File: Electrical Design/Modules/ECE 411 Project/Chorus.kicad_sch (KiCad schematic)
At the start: 42 parts, among them Q2 2N3904, Q3 2N3904, Q4 2N3904, U3 MN3207

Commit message: kicad business
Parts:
- renumbered V3207D to V3207D1, V3207D to V3207D2
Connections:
- net +V: no longer Q2.3 (C)
- net GND: now also R22.1
- new net 9V: Q2.3 (C)
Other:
- company: (none) -> Portland State University
- title: (none) -> Chorus Effect
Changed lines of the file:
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@@
 	(generator_version "8.0")
 	(paper "A4")
+	(title_block
+		(title "Chorus Effect")
+		(date "2024-10-31")
+		(rev "1.1")
+		(company "Portland State University")
+		(comment 1 "Open Source Hardware")
+		(comment 2 "Design: Eric Sanman, Sierra Buckley, Chuong Vo, Chris Crider")
+	)
 	(junction
 		(at 92.71 41.91)
@@
 		)
 	)
-	(global_label "+V"
-		(shape input)
-		(at 50.8 19.05 90)
-		(fields_autoplaced yes)
-		(effects
-			(font
-				(size 1.27 1.27)
-			)
-			(justify left)
-		)
-		(property "Intersheetrefs" "${INTERSHEET_REFS}"
-			(at 50.8 13.4038 90)
-			(effects
-				(font
-					(size 1.27 1.27)
-				)
-				(justify left)
-				(hide yes)
-			)
-		)
-	)
 	(global_label "Clock{slash}lfo from .uC"
 		(shape input)
@@
 		)
 	)
+	(hierarchical_label "9V"
+		(shape input)
+		(at 50.8 19.05 90)
+		(fields_autoplaced yes)
+		(effects
+			(font
+				(size 1.27 1.27)
+			)
+			(justify left)
+		)
+	)
 	(symbol
 		(lib_id "Device:R")
@@
 		(dnp no)
 		(fields_autoplaced yes)
-		(property "Reference" "V3207D"
+		(property "Reference" "V3207D2"
 			(at 156.21 141.0014 0)
 			(effects
@@
 			(project "ECE 411 Project"
 				(path "/2625e5a1-d0c8-41ce-941d-75d035a5f1c5/9b94327a-6b02-4c1c-b4e8-ca4e897770fe"
-					(reference "V3207D")
+					(reference "V3207D2")
 					(unit 1)
 				)
@@
 	)
 	(symbol
+		(lib_id "power:GND")
+		(at 133.35 69.85 0)
+		(unit 1)
+		(exclude_from_sim no)
+		(in_bom yes)
+		(on_board yes)
+		(dnp no)
+		(fields_autoplaced yes)
+		(property "Reference" "#PWR044"
+			(at 133.35 76.2 0)
+			(effects
+				(font
+					(size 1.27 1.27)
+				)
+				(hide yes)
+			)
+		)
+		(property "Value" "GND"
+			(at 133.35 74.93 0)
+			(effects
+				(font
+					(size 1.27 1.27)
+				)
+			)
+		)
+		(property "Footprint" ""
+			(at 133.35 69.85 0)
+			(effects
+				(font
+					(size 1.27 1.27)
+				)
+				(hide yes)
+			)
+		)
+		(property "Datasheet" ""
+			(at 133.35 69.85 0)
+			(effects
+				(font
+					(size 1.27 1.27)
+				)
+				(hide yes)
+			)
+		)
+		(property "Description" "Power symbol creates a global label with name \"GND\" , ground"
+			(at 133.35 69.85 0)
+			(effects
+				(font
+					(size 1.27 1.27)
+				)
+				(hide yes)
+			)
+		)
+		(pin "1"
+		)
+		(instances
+			(project ""
+				(path "/2625e5a1-d0c8-41ce-941d-75d035a5f1c5/9b94327a-6b02-4c1c-b4e8-ca4e897770fe"
+					(reference "#PWR044")
+					(unit 1)
+				)
+			)
+		)
+	)
+	(symbol
 		(lib_id "Device:R")
 		(at 92.71 57.15 180)
@@
 		(on_board yes)
 		(dnp no)
-		(property "Reference" "V3207D"
+		(property "Reference" "V3207D1"
 			(at 110.236 39.37 0)
 			(effects
@@
 			(project ""
 				(path "/2625e5a1-d0c8-41ce-941d-75d035a5f1c5/9b94327a-6b02-4c1c-b4e8-ca4e897770fe"
-					(reference "V3207D")
+					(reference "V3207D1")
 					(unit 1)
 				)

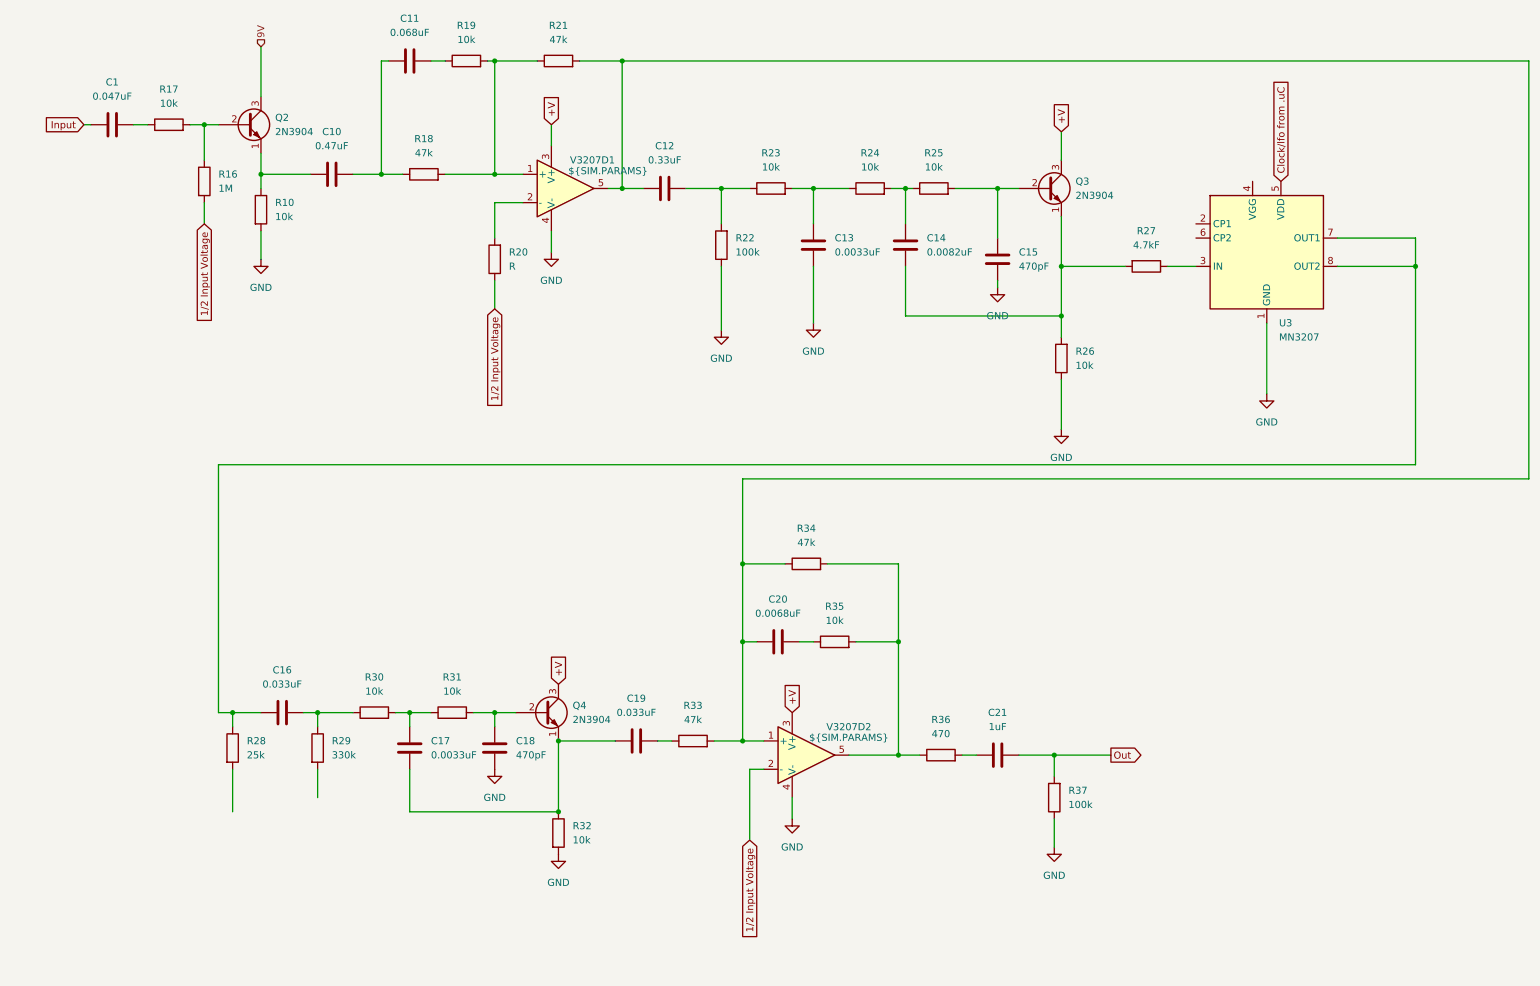
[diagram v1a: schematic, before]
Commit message: add psu and fix schematic
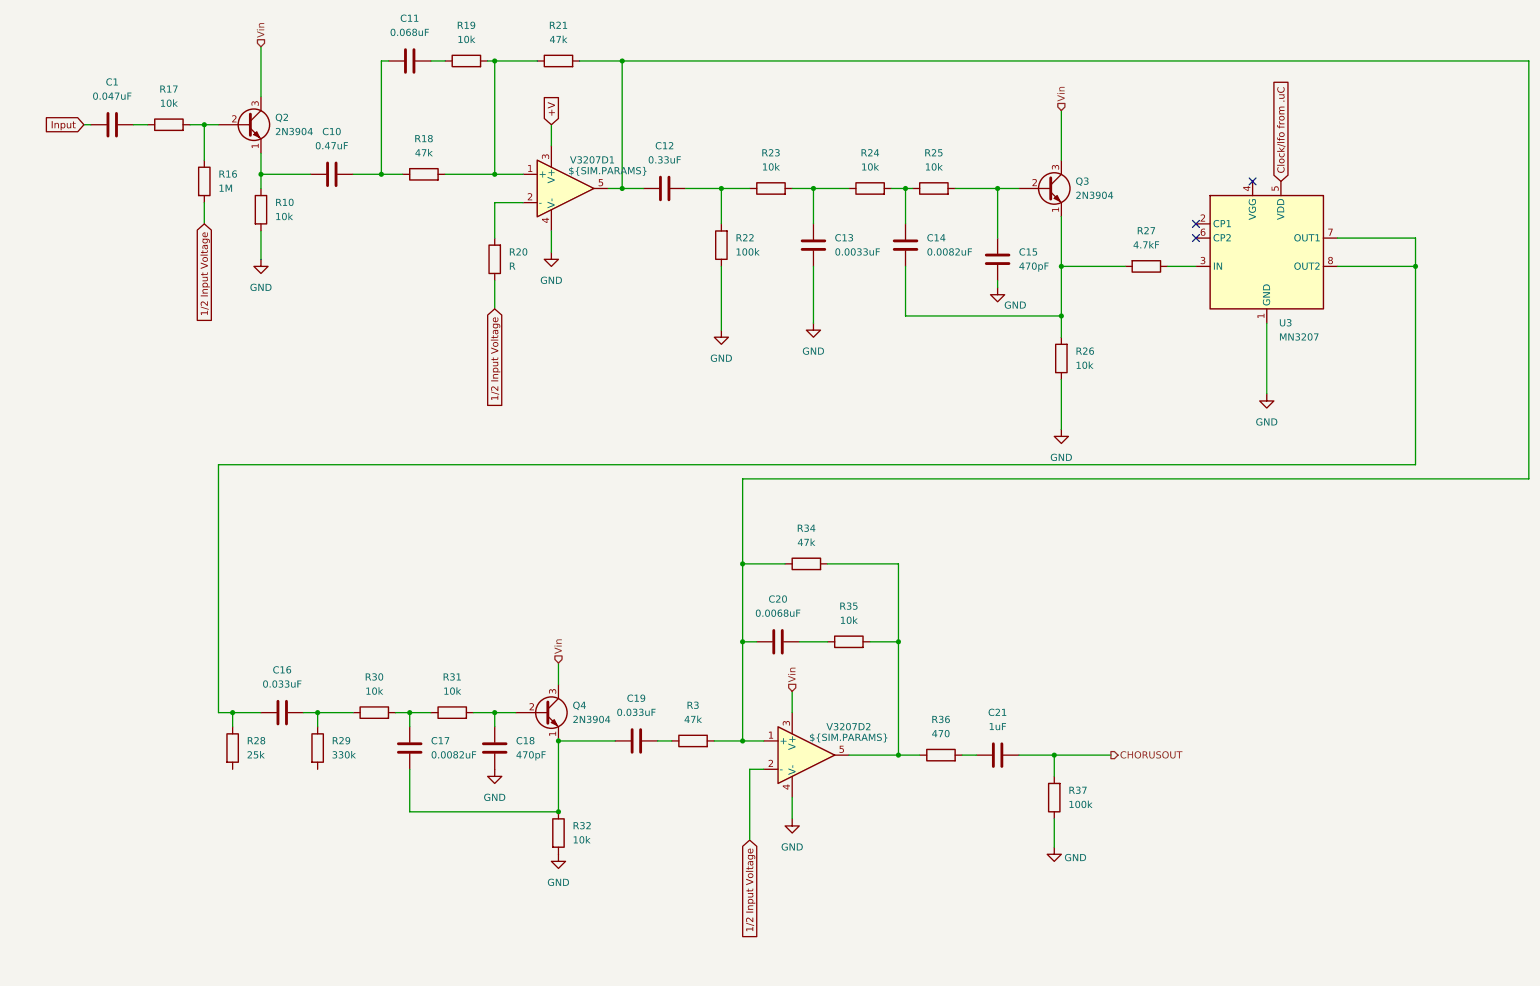
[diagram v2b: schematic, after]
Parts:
- removed R33: 47k, symbol Device:R
- added R3: 47k, symbol Device:R
- C17: value 0.0033uF -> 0.0082uF
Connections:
- net +V: no longer Q3.3 (C), Q4.3 (C), V3207D2.3 (V+)
- net at C12.1, C20.1, R21.2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: now also R3.2
- net at R34.2, R36.1, V3207D2.5: now also R35.2
- net at C19.2: now also R3.1
- net at C20.2: now also R35.1
- net 9V renamed Vin
- net Vin: now also Q3.3 (C), Q4.3 (C), V3207D2.3 (V+)
- net Out renamed CHORUSOUT
- no-connect marks 0 -> 3

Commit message: filter changes
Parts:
- removed R29: 330k, symbol Device:R
- added C41: 0.0033uF, symbol Device:C
- added R6: 10k, symbol Device:R
- added R7: 47k, symbol Device:R
- added R8: 56k, symbol Device:R
- C16: value 0.033uF -> 0.033u
- R20: value R -> 10k
- R28: value 25k -> 330k
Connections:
- net 1/2 Input Voltage: now also R28.2
- net GND: now also C41.2, R8.2
- net at C20.1, R3.2, R34.1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: now also R7.2; no longer C12.1, R21.2, V3207D1.5
- net at C16.2: now also R28.1, R6.2; no longer R30.1
- net at C16.1, U3.7 (OUT1), U3.8 (OUT2): now also R8.1; no longer R28.1
- new net: C41.1, R30.1, R6.1
- new net: C12.1, R21.2, R7.1, V3207D1.5

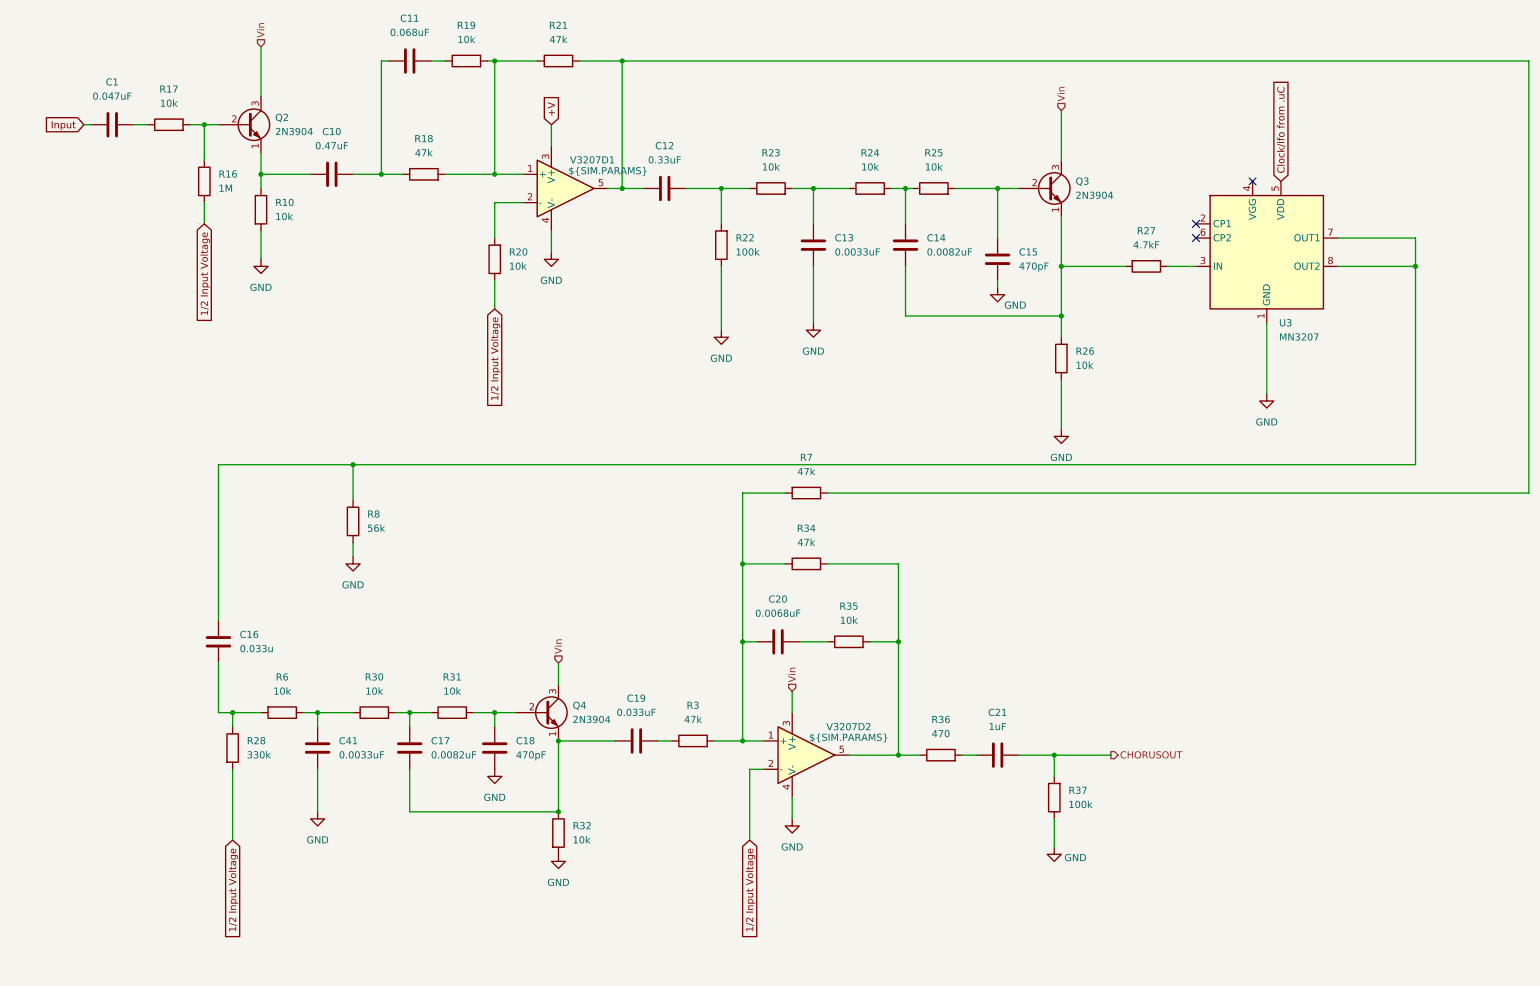
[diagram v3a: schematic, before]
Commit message: schematic, start layout
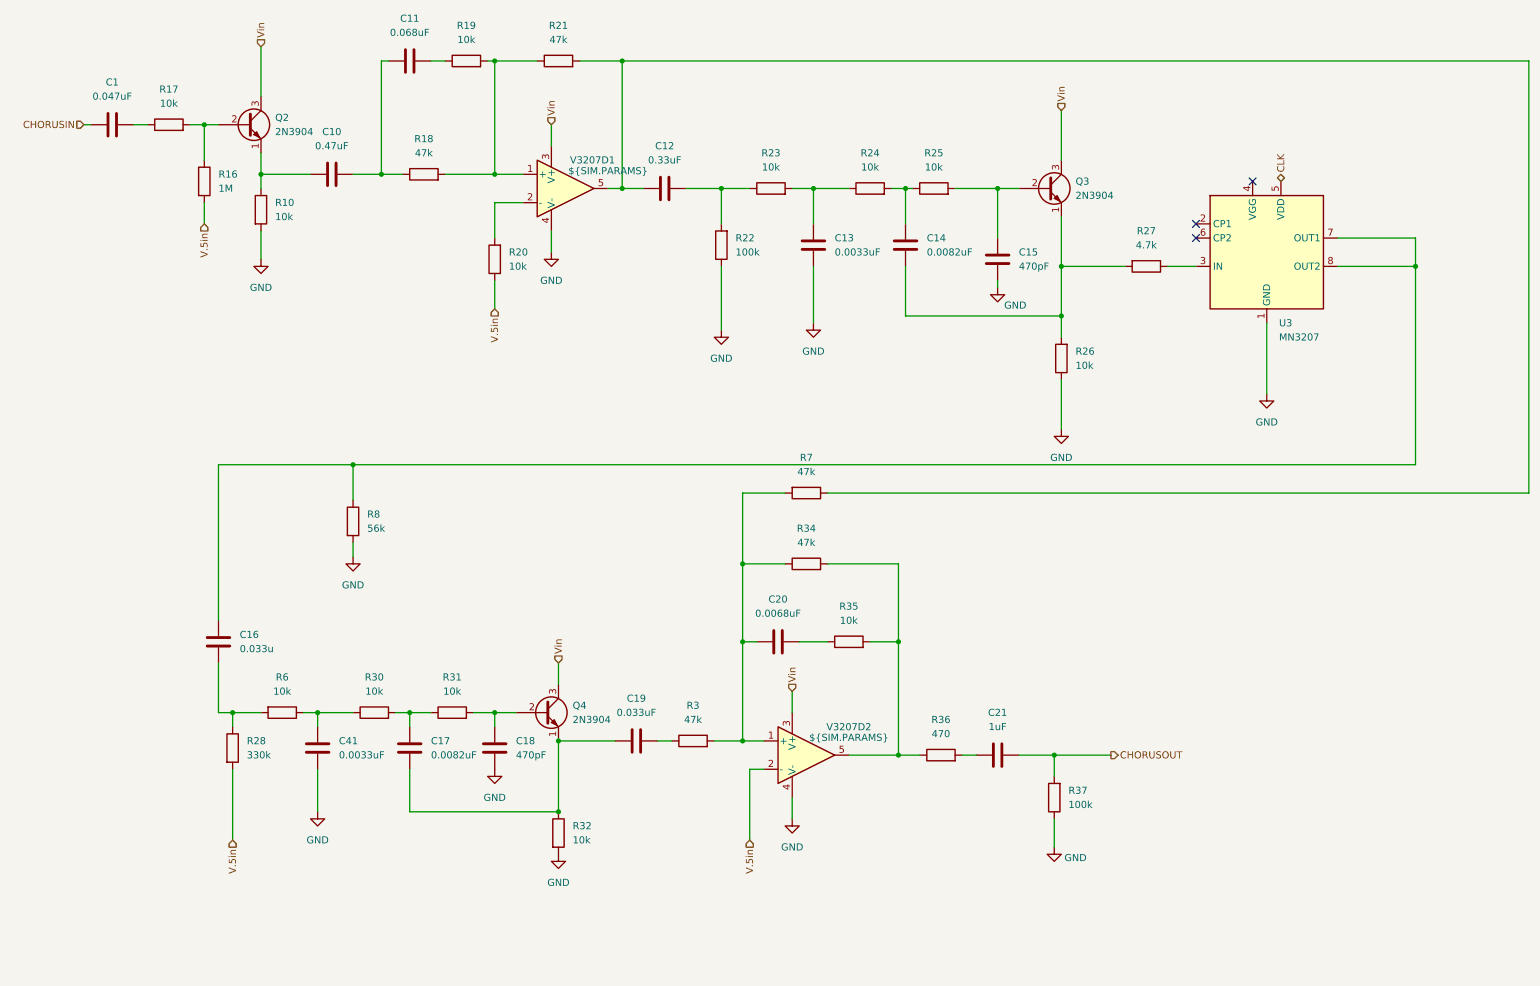
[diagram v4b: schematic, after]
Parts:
- C1, C10, C11, C12, C13, C14, C15, C16, C17, C18, C19, C20, C21, C41: footprint (none) -> Capacitor_SMD:C_0805_2012Metric_Pad1.18x1.45mm_HandSolder
- R10, R16, R17, R18, R19, R20, R21, R22, R23, R24, R25, R26, R28, R3, R30, R31, R32, R34, R35, R36, R37, R6, R7, R8: footprint (none) -> Resistor_SMD:R_0805_2012Metric_Pad1.20x1.40mm_HandSolder
- R27: value 4.7kF -> 4.7k; footprint (none) -> Resistor_SMD:R_0805_2012Metric_Pad1.20x1.40mm_HandSolder
- U3, V3207D1, V3207D2: footprint (none) -> Package_DIP:CERDIP-8_W7.62mm_SideBrazed
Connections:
- net +V is gone; now on net Vin: V3207D1.3 (V+)
- net 1/2 Input Voltage renamed V.5in
- net Clock/lfo from .uC renamed CLK
- net Input renamed CHORUSIN

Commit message: update BOM
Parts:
- C1: value 0.047uF -> 47nF; On Hand (On Way) (none) -> (100); Part Number (none) -> CL21B473KBCNNNC; Part Origin (none) -> DK
- C10: On Hand (On Way) (none) -> (100); Part Number (none) -> CL21B473KBCNNNC; Part Origin (none) -> DK
- C11: value 0.068uF -> 68nF; On Hand (On Way) (none) -> (100); Part Number (none) -> KGM21NR71H683KT; Part Origin (none) -> DK
- C12: On Hand (On Way) (none) -> (100); Part Number (none) -> CL21B334KBFNNNE; Part Origin (none) -> DK
- C13, C41: value 0.0033uF -> 3.3nF; On Hand (On Way) (none) -> (50); Part Number (none) -> C0805C332K1RECAUTO; Part Origin (none) -> DK
- C14, C17: value 0.0082uF -> 8.2nF; On Hand (On Way) (none) -> (50); Part Number (none) -> C0402C822K1RACAUTO; Part Origin (none) -> DK
- C15, C18: On Hand (On Way) (none) -> (100); Part Number (none) -> C0805C471K5RAC7800; Part Origin (none) -> DK
- C16: value 0.033u -> 33nF; On Hand (On Way) (none) -> (50); Part Number (none) -> C0805C333K1RECAUTO; Part Origin (none) -> DK
- C19: value 0.033uF -> 33nF; On Hand (On Way) (none) -> (50); Part Number (none) -> C0805C333K1RECAUTO; Part Origin (none) -> DK
- C20: value 0.0068uF -> 6.8nF; Part Origin (none) -> DK
- C21, R10, R16, R17, R18, R19, R20, R21, R22, R23, R24, R25, R26, R27, R28, R3, R30, R31, R32, R34, R35, R36, R37, R6, R7, R8: Part Origin (none) -> DK
- U3, V3207D1, V3207D2: Part Origin (none) -> SBP
